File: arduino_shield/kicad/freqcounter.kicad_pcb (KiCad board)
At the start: 2 copper layers, 47 x 53.3 mm, 38 parts, among them J1 ICSP, J2 UART, J3 INPUT CLK, J4 INPUT A, J5 INPUT B, J6 INPUT ZCD, J7 POWER, J8 ICSP2, P1 LCD_DISPLAY_16X2, U1 PIC16F18446, Y1 Crystal

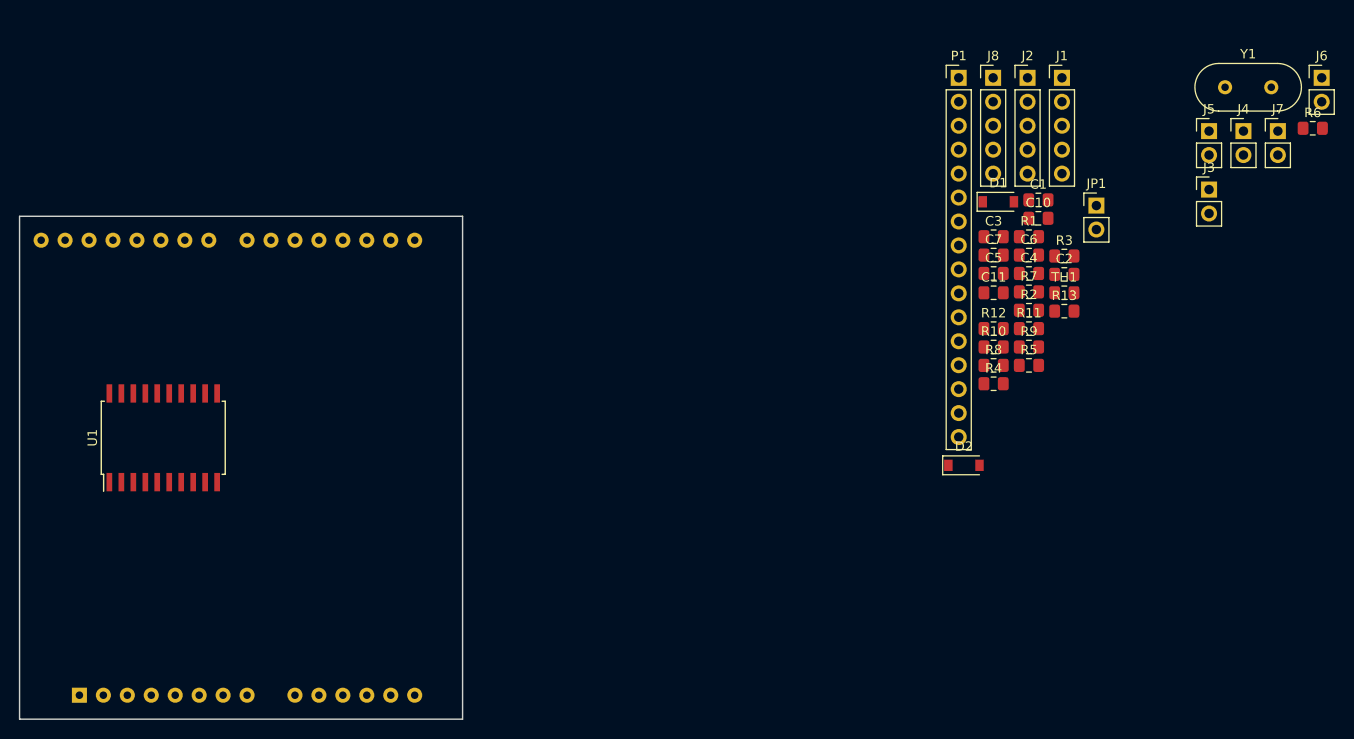
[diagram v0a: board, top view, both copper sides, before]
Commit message: Updated Arduino shield schematic and PCB
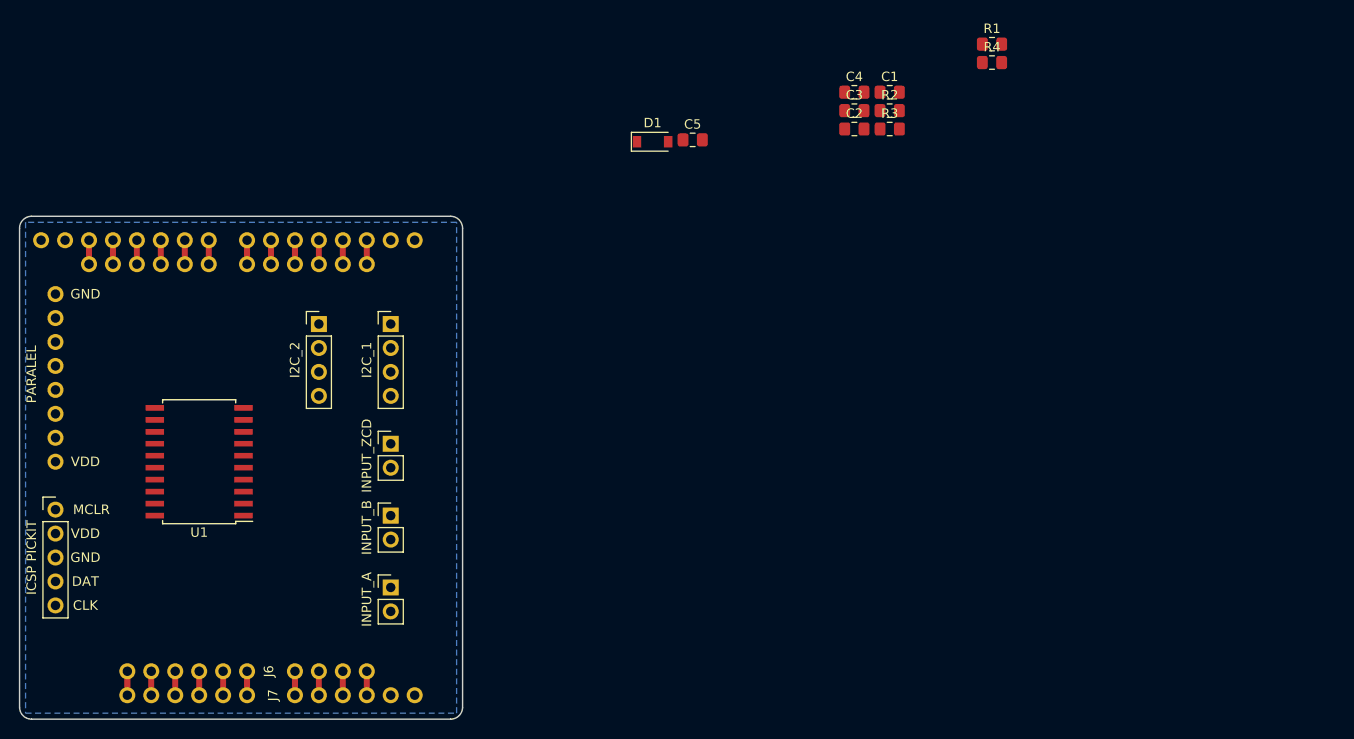
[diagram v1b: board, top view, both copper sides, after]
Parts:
- removed C10, C6: 100nF, Capacitor_SMD:C_0805_2012Metric_Pad1.15x1.40mm_HandSolder
- removed C11, C7: 10uF, Capacitor_SMD:C_0805_2012Metric_Pad1.15x1.40mm_HandSolder
- removed D2: 1N4148W, Diode_SMD:D_SOD-123
- removed JP1: Jumper, Connector_PinHeader_2.54mm:PinHeader_1x02_P2.54mm_Vertical
- removed P1: LCD_DISPLAY_16X2, Connector_PinHeader_2.54mm:PinHeader_1x16_P2.54mm_Vertical
- removed R10, R8: 220, Resistor_SMD:R_0805_2012Metric_Pad1.15x1.40mm_HandSolder
- removed R11, R12, R6, R7: 180, Resistor_SMD:R_0805_2012Metric_Pad1.15x1.40mm_HandSolder
- removed R13: 10M, Resistor_SMD:R_0805_2012Metric_Pad1.15x1.40mm_HandSolder
- removed R5: 10k, Resistor_SMD:R_0805_2012Metric_Pad1.15x1.40mm_HandSolder
- removed R9: 10K, Resistor_SMD:R_0805_2012Metric_Pad1.15x1.40mm_HandSolder
- removed REF**: Arduino_UNO_R2, Module:Arduino_UNO_R2
- removed TH1: NTC 10K, Resistor_SMD:R_0805_2012Metric_Pad1.15x1.40mm_HandSolder
- removed Y1: Crystal, Crystal:Crystal_HC18-U_Vertical
- added J10: INPUT_A, Connector_PinHeader_2.54mm:PinHeader_1x02_P2.54mm_Vertical, F.Cu at (160.0, 96.5)
- added J11: INPUT_B, Connector_PinHeader_2.54mm:PinHeader_1x02_P2.54mm_Vertical, F.Cu at (160.0, 88.9)
- added J12: INPUT_ZCD, Connector_PinHeader_2.54mm:PinHeader_1x02_P2.54mm_Vertical, F.Cu at (160.0, 81.3)
- added J13: I2C_1, Connector_PinHeader_2.54mm:PinHeader_1x04_P2.54mm_Vertical, F.Cu at (160.0, 68.6)
- added J14: I2C_2, Connector_PinHeader_2.54mm:PinHeader_1x04_P2.54mm_Vertical, F.Cu at (152.4, 68.6)
- added J15: PARALEL, Footprints:Connector_1x08, F.Cu at (124.5, 83.2)
- added J9: Arduino_Digital_1, Footprints:Connector_1x08, F.Cu at (144.8, 59.7)
- C1: value 2.2nF -> 10uF
- C2: value 22pF -> 100nF
- C3: value 22pF -> 2.2nF
- D1: value 1N4148W -> 1N4148
- J1: value ICSP -> ICSP PICKIT
- J2: value UART -> Arduino_Power; footprint Connector_PinHeader_2.54mm:PinHeader_1x05_P2.54mm_Vertical -> Footprints:Connector_1x06
- J3: value INPUT CLK -> Arduino_Power; footprint Connector_PinHeader_2.54mm:PinHeader_1x02_P2.54mm_Vertical -> Footprints:Connector_1x06
- J4: value INPUT A -> Arduino_Digital_2; footprint Connector_PinHeader_2.54mm:PinHeader_1x02_P2.54mm_Vertical -> Footprints:Connector_1x08
- J5: value INPUT B -> Digital_2; footprint Connector_PinHeader_2.54mm:PinHeader_1x02_P2.54mm_Vertical -> Footprints:Connector_1x06
- J6: value INPUT ZCD -> Analog; footprint Connector_PinHeader_2.54mm:PinHeader_1x02_P2.54mm_Vertical -> Footprints:Connector_1x04
- J7: value POWER -> Arduino_Analog; footprint Connector_PinHeader_2.54mm:PinHeader_1x02_P2.54mm_Vertical -> Footprints:Connector_1x06
- J8: value ICSP2 -> Digital_1; footprint Connector_PinHeader_2.54mm:PinHeader_1x05_P2.54mm_Vertical -> Footprints:Connector_1x06
- R1: value 1K -> 10K
- R3: value 180 -> 1K
- R4: value 10K -> 1M
- moved J4 128.1 mm to (122.9, 59.7), turned to 90 degrees
- moved J6 125.8 mm to (149.9, 105.4), turned to 90 degrees
- moved J3 125.6 mm to (132.1, 105.4), turned to 90 degrees
- moved J7 120.2 mm to (149.9, 108.0), turned to 90 degrees
- moved J5 119.6 mm to (128.0, 62.2), turned to 90 degrees
- moved J1 116.2 mm to (124.5, 88.3)
- moved J2 115.8 mm to (132.1, 108.0), turned to 90 degrees
- moved J8 81.6 mm to (144.8, 62.2), turned to 90 degrees
- moved D1 37.2 mm to (187.8, 49.2)
- moved C5 34.9 mm to (192.0, 49.0)
- moved R4 34.1 mm to (223.8, 40.8)
- moved C2 27.1 mm to (209.2, 47.9)
- moved C4 26.7 mm to (209.2, 44.0)
- moved R2 25.8 mm to (212.9, 45.9)
- moved R3 22.9 mm to (212.9, 47.9)
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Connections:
- C1 pad 1: DTIME -> GND
- C1 pad 2: GND -> 5V
- C2 pad 1: CLKIN2 -> GND
- C2 pad 2: GND -> 5V
- C3 pad 2: GND -> Earth
- C4 pad 1: MCLR -> Net-(C4-Pad1)
- C4 pad 2: GND -> 32MHz
- C5 pad 2: VDD -> 3.3V
- D1 pad 1: Net-(D1-Pad1) -> Net-(C3-Pad1)
- D1 pad 2: MCLR -> Net-(D1-Pad2)
- J1 pad 4: PGD -> ICSPDAT
- J1 pad 5: PGC -> ICSPCLK
- J2 pad 1: GND -> Reset
- J2 pad 2: Net-(J2-Pad2) -> 3.3V
- J2 pad 3: Net-(J2-Pad3) -> 5V
- J2 pad 4: Net-(D1-Pad1) -> GND
- J2 pad 5: VDD -> GND
- J3 pad 1: Net-(J3-Pad1) -> Reset
- J3 pad 2: GND -> 3.3V
- J5 pad 1: Net-(J5-Pad1) -> Net-(J4-Pad3)
- J5 pad 2: GND -> Net-(J4-Pad4)
- J6 pad 2: GND -> Net-(J6-Pad2)
- J7 pad 1: Net-(C8-Pad1) -> Net-(J6-Pad1)
- J7 pad 2: GND -> Net-(J6-Pad2)
- J8 pad 1: MCLR2 -> Net-(J8-Pad1)
- J8 pad 2: VDD -> Net-(J8-Pad2)
- J8 pad 3: GND -> Net-(J8-Pad3)
- J8 pad 4: PGD -> Net-(J8-Pad4)
- J8 pad 5: PGC -> Net-(J8-Pad5)
- R1 pad 1: DISP -> INPUT_ZCD
- R1 pad 2: Net-(D2-Pad2) -> Net-(R1-Pad2)
- R2 pad 1: INPUT_A -> ARD_TX
- R2 pad 2: Net-(J4-Pad1) -> Net-(R2-Pad2)
- R3 pad 1: INPUT_B -> Net-(R3-Pad1)
- R3 pad 2: Net-(J5-Pad1) -> Net-(D1-Pad2)
- R4 pad 1: ZCD -> Net-(D1-Pad2)
- R4 pad 2: Net-(J6-Pad1) -> Net-(C3-Pad1)
- U1 pad 1: VDD -> 5V
- U1 pad 10: LCD_D7 -> P1
- U1 pad 11: LCD_D5 -> P2
- U1 pad 12: LCD_D4 -> P3
- U1 pad 13: LCD_E -> SCL
- U1 pad 14: LCD_RS -> SDA
- U1 pad 15: RX1 -> ARD_RX
- U1 pad 16: TX1 -> Net-(R2-Pad2)
- U1 pad 17: ZCD -> Net-(R1-Pad2)
- U1 pad 18: PGC -> ICSPCLK
- U1 pad 19: PGD -> ICSPDAT
- U1 pad 2: CLKIN2 -> 32MHz
- U1 pad 3: CLKOUT -> Net-(U1-Pad3)
- U1 pad 5: INPUT_A2 -> INPUT_A
- U1 pad 6: INPUT_B2 -> INPUT_B
- U1 pad 7: DTIME -> Net-(C3-Pad1)
- U1 pad 8: DISP -> Net-(R3-Pad1)
- U1 pad 9: LCD_D6 -> P0
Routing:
- net GND: track 0.00 -> 5.08 mm
- net Vin: track 0.00 -> 2.54 mm
- net Reset: track 0.00 -> 2.54 mm
- net Net-(J6-Pad4): track 0.00 -> 2.54 mm
- net Net-(J6-Pad3): track 0.00 -> 2.54 mm
- net Net-(J6-Pad2): track 0.00 -> 2.54 mm
- net Net-(J6-Pad1): track 0.00 -> 2.54 mm
- net 5V: track 0.00 -> 2.54 mm
- net 3.3V: track 0.00 -> 2.54 mm
- net Net-(J8-Pad6): track 0.00 -> 2.54 mm
- net Net-(J8-Pad5): track 0.00 -> 2.54 mm
- net Net-(J8-Pad4): track 0.00 -> 2.54 mm
- net Net-(J8-Pad3): track 0.00 -> 2.54 mm
- net Net-(J8-Pad2): track 0.00 -> 2.54 mm
- net Net-(J8-Pad1): track 0.00 -> 2.54 mm
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- added copper zone on B.Cu, net GND
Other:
- outline, holes or cut-outs redrawn
- board text added: "CLK"
- board text added: "DAT"
- board text added: "GND"
- board text added: "MCLR"
- board text added: "VDD"
